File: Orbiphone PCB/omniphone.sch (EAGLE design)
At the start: 45 parts

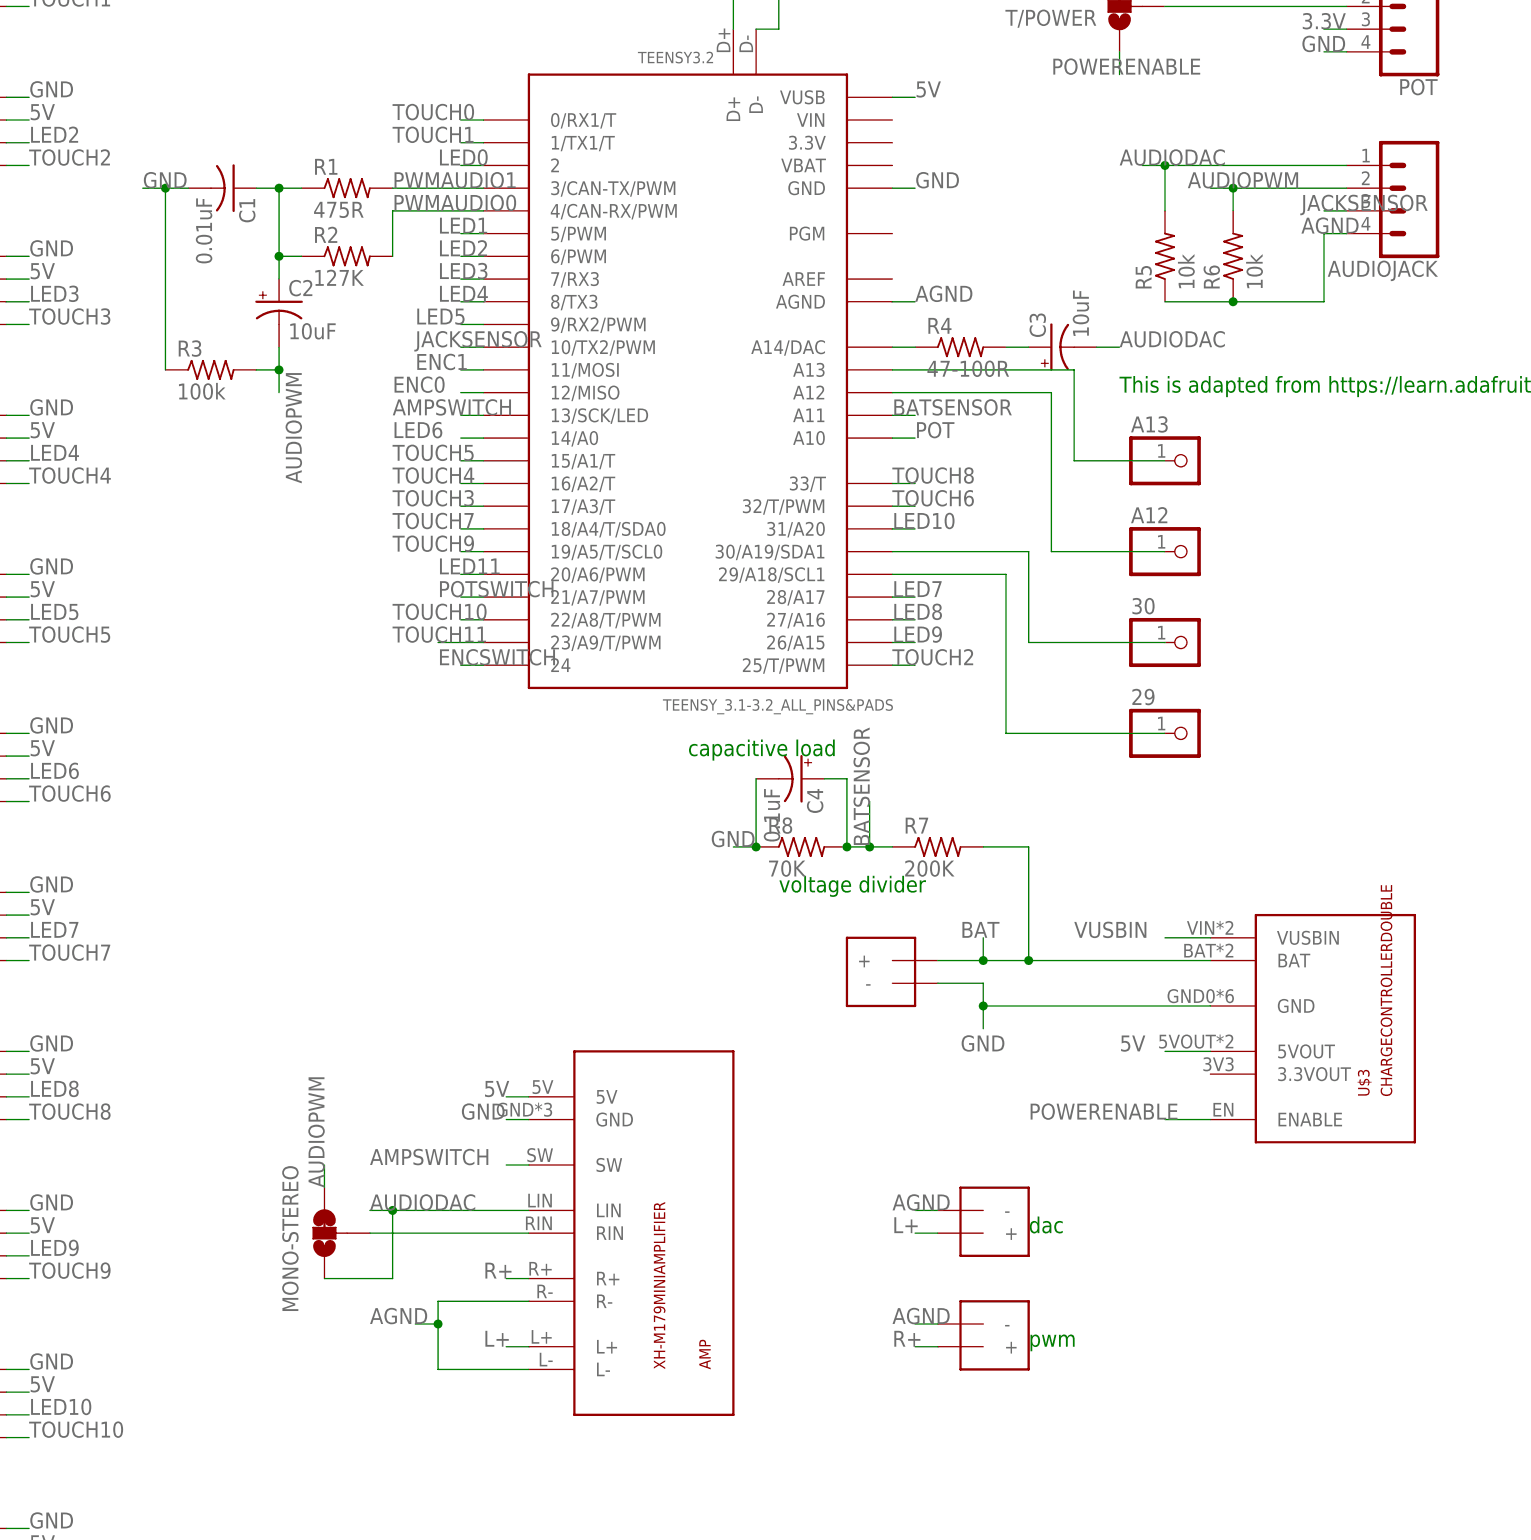
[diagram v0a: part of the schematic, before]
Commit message: added speaker and headphone fixes
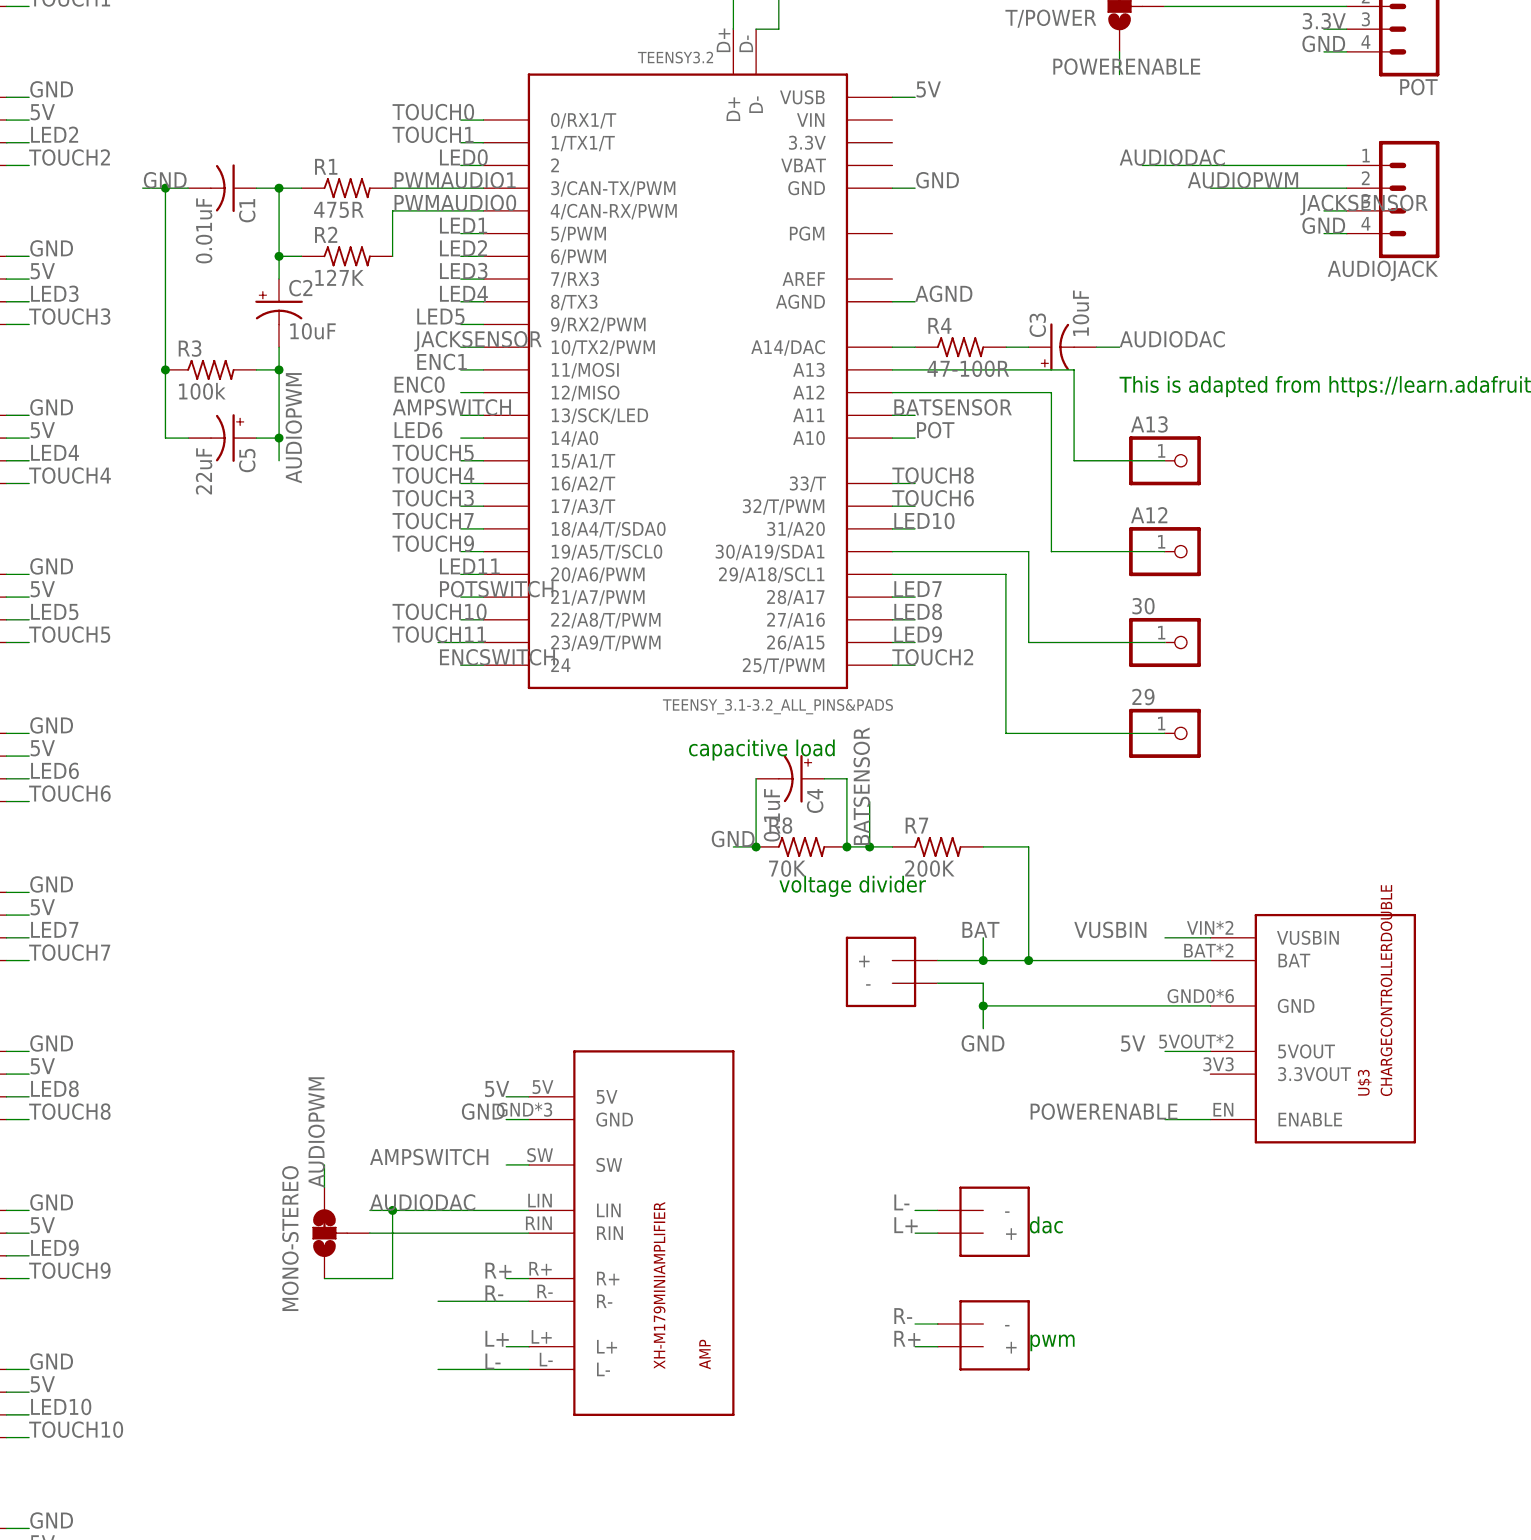
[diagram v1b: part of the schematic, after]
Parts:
- removed R5, R6: 10k, adafruit:R-US_0204/2V
- added C5: 22uF, adafruit:CPOL-USE2-4
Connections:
- new net L-: AMP.L-, SPEAKERDAC.-
- new net R-: AMP.R-, SPEAKERPWM.-
- net AGND: no longer AMP.L-, AMP.R-, AUDIOJACK.4, R5.1, R6.1, SPEAKERDAC.-, SPEAKERPWM.-
- net AUDIODAC: no longer R5.2
- net AUDIOPWM: now also C5.+; no longer R6.2
- net GND: now also AUDIOJACK.4, C5.-
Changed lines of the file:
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@@
 <part name="C3" library="adafruit" library_urn="urn:adsk.eagle:library:420" deviceset="CPOL-US" device="E2-4" package3d_urn="urn:adsk.eagle:package:6240495/1" value="10uF"/>
 <part name="R4" library="adafruit" library_urn="urn:adsk.eagle:library:420" deviceset="R-US_" device="0204/2V" package3d_urn="urn:adsk.eagle:package:6240630/1" value="47-100R"/>
-<part name="R5" library="adafruit" library_urn="urn:adsk.eagle:library:420" deviceset="R-US_" device="0204/2V" package3d_urn="urn:adsk.eagle:package:6240630/1" value="10k"/>
-<part name="R6" library="adafruit" library_urn="urn:adsk.eagle:library:420" deviceset="R-US_" device="0204/2V" package3d_urn="urn:adsk.eagle:package:6240630/1" value="10k"/>
 <part name="MONO-STEREO" library="SparkFun-Jumpers" library_urn="urn:adsk.eagle:library:528" deviceset="JUMPER-SMT_3_1-NC_TRACE" device="_SILK" package3d_urn="urn:adsk.eagle:package:39288/1"/>
 <part name="SPEAKERDAC" library="ArvidLibrary" deviceset="SPEAKERTERMINAL" device="-3.5MM" package3d_urn="urn:adsk.eagle:package:6240635/1"/>
@@
 <part name="30" library="adafruit" library_urn="urn:adsk.eagle:library:420" deviceset="PINHD-1X1" device="" package3d_urn="urn:adsk.eagle:package:6240654/1"/>
 <part name="29" library="adafruit" library_urn="urn:adsk.eagle:library:420" deviceset="PINHD-1X1" device="" package3d_urn="urn:adsk.eagle:package:6240654/1"/>
+<part name="C5" library="adafruit" library_urn="urn:adsk.eagle:library:420" deviceset="CPOL-US" device="E2-4" package3d_urn="urn:adsk.eagle:package:6240495/1" value="22uF"/>
 </parts>
 <sheets>
@@
 <attribute name="VALUE" x="90.17" y="60.198" size="1.778" layer="96"/>
 </instance>
-<instance part="R5" gate="G$1" x="116.84" y="73.66" smashed="yes" rot="R90">
-<attribute name="NAME" x="115.3414" y="69.85" size="1.778" layer="95" rot="R90"/>
-<attribute name="VALUE" x="120.142" y="69.85" size="1.778" layer="96" rot="R90"/>
-</instance>
-<instance part="R6" gate="G$1" x="124.46" y="73.66" smashed="yes" rot="R90">
-<attribute name="NAME" x="122.9614" y="69.85" size="1.778" layer="95" rot="R90"/>
-<attribute name="VALUE" x="127.762" y="69.85" size="1.778" layer="96" rot="R90"/>
-</instance>
 <instance part="MONO-STEREO" gate="G$1" x="22.86" y="-35.56" smashed="yes" rot="R180">
 <attribute name="NAME" x="18.161" y="-27.94" size="1.778" layer="95" font="vector" rot="R270"/>
@@
 <attribute name="NAME" x="113.03" y="23.495" size="1.778" layer="95"/>
 <attribute name="VALUE" x="113.03" y="15.24" size="1.778" layer="96"/>
+</instance>
+<instance part="C5" gate="G$1" x="12.7" y="53.34" smashed="yes" rot="R270">
+<attribute name="NAME" x="13.335" y="52.324" size="1.778" layer="95" rot="R270"/>
+<attribute name="VALUE" x="8.509" y="52.324" size="1.778" layer="96" rot="R270"/>
 </instance>
 </instances>
@@
 <junction x="5.08" y="81.28"/>
 <label x="2.54" y="81.28" size="1.778" layer="95"/>
+<pinref part="C5" gate="G$1" pin="-"/>
+<wire x1="7.62" y1="53.34" x2="5.08" y2="53.34" width="0.1524" layer="91"/>
+<wire x1="5.08" y1="53.34" x2="5.08" y2="60.96" width="0.1524" layer="91"/>
+<junction x="5.08" y="60.96"/>
 </segment>
 <segment>
@@
 <wire x1="71.12" y1="15.24" x2="71.12" y2="7.62" width="0.1524" layer="91"/>
 <junction x="71.12" y="7.62"/>
+</segment>
+<segment>
+<pinref part="AUDIOJACK" gate="G$1" pin="4"/>
+<wire x1="137.16" y1="76.2" x2="134.62" y2="76.2" width="0.1524" layer="91"/>
+<label x="132.08" y="76.2" size="1.778" layer="95"/>
 </segment>
 </net>
@@
 <pinref part="C2" gate="G$1" pin="-"/>
 <wire x1="17.78" y1="63.5" x2="17.78" y2="60.96" width="0.1524" layer="91"/>
-<wire x1="17.78" y1="60.96" x2="17.78" y2="58.42" width="0.1524" layer="91"/>
 <wire x1="17.78" y1="60.96" x2="15.24" y2="60.96" width="0.1524" layer="91"/>
 <junction x="17.78" y="60.96"/>
 <pinref part="R3" gate="G$1" pin="2"/>
 <label x="20.32" y="48.26" size="1.778" layer="95" rot="R90"/>
+<pinref part="C5" gate="G$1" pin="+"/>
+<wire x1="17.78" y1="60.96" x2="17.78" y2="53.34" width="0.1524" layer="91"/>
+<wire x1="17.78" y1="53.34" x2="15.24" y2="53.34" width="0.1524" layer="91"/>
+<wire x1="17.78" y1="53.34" x2="17.78" y2="50.8" width="0.1524" layer="91"/>
+<junction x="17.78" y="53.34"/>
 </segment>
 <segment>
 <pinref part="AUDIOJACK" gate="G$1" pin="2"/>
 <label x="119.38" y="81.28" size="1.778" layer="95"/>
-<pinref part="R6" gate="G$1" pin="2"/>
-<wire x1="137.16" y1="81.28" x2="124.46" y2="81.28" width="0.1524" layer="91"/>
-<wire x1="124.46" y1="81.28" x2="124.46" y2="78.74" width="0.1524" layer="91"/>
-<wire x1="124.46" y1="81.28" x2="121.92" y2="81.28" width="0.1524" layer="91"/>
-<junction x="124.46" y="81.28"/>
+<wire x1="137.16" y1="81.28" x2="121.92" y2="81.28" width="0.1524" layer="91"/>
 </segment>
 <segment>
@@
 <pinref part="AUDIOJACK" gate="G$1" pin="1"/>
 <label x="111.76" y="83.82" size="1.778" layer="95"/>
-<pinref part="R5" gate="G$1" pin="2"/>
-<wire x1="137.16" y1="83.82" x2="116.84" y2="83.82" width="0.1524" layer="91"/>
-<wire x1="116.84" y1="83.82" x2="116.84" y2="78.74" width="0.1524" layer="91"/>
-<wire x1="116.84" y1="83.82" x2="114.3" y2="83.82" width="0.1524" layer="91"/>
-<junction x="116.84" y="83.82"/>
+<wire x1="137.16" y1="83.82" x2="114.3" y2="83.82" width="0.1524" layer="91"/>
 </segment>
 <segment>
@@
 <wire x1="86.36" y1="68.58" x2="88.9" y2="68.58" width="0.1524" layer="91"/>
 <label x="88.9" y="68.58" size="1.778" layer="95"/>
-</segment>
-<segment>
-<pinref part="AMP" gate="G$1" pin="L-"/>
-<wire x1="45.72" y1="-50.8" x2="35.56" y2="-50.8" width="0.1524" layer="91"/>
-<pinref part="AMP" gate="G$1" pin="R-"/>
-<wire x1="35.56" y1="-50.8" x2="35.56" y2="-45.72" width="0.1524" layer="91"/>
-<wire x1="35.56" y1="-45.72" x2="35.56" y2="-43.18" width="0.1524" layer="91"/>
-<wire x1="35.56" y1="-43.18" x2="45.72" y2="-43.18" width="0.1524" layer="91"/>
-<wire x1="35.56" y1="-45.72" x2="33.02" y2="-45.72" width="0.1524" layer="91"/>
-<junction x="35.56" y="-45.72"/>
-<label x="27.94" y="-45.72" size="1.778" layer="95"/>
-</segment>
-<segment>
-<pinref part="AUDIOJACK" gate="G$1" pin="4"/>
-<wire x1="137.16" y1="76.2" x2="134.62" y2="76.2" width="0.1524" layer="91"/>
-<label x="132.08" y="76.2" size="1.778" layer="95"/>
-<pinref part="R6" gate="G$1" pin="1"/>
-<wire x1="124.46" y1="68.58" x2="134.62" y2="68.58" width="0.1524" layer="91"/>
-<wire x1="134.62" y1="68.58" x2="134.62" y2="76.2" width="0.1524" layer="91"/>
-<pinref part="R5" gate="G$1" pin="1"/>
-<wire x1="124.46" y1="68.58" x2="116.84" y2="68.58" width="0.1524" layer="91"/>
-<junction x="124.46" y="68.58"/>
-</segment>
-<segment>
-<pinref part="SPEAKERPWM" gate="&gt;NAME" pin="-"/>
-<wire x1="91.44" y1="-45.72" x2="88.9" y2="-45.72" width="0.1524" layer="91"/>
-<label x="86.36" y="-45.72" size="1.778" layer="95"/>
-</segment>
-<segment>
-<pinref part="SPEAKERDAC" gate="&gt;NAME" pin="-"/>
-<wire x1="91.44" y1="-33.02" x2="88.9" y2="-33.02" width="0.1524" layer="91"/>
-<label x="86.36" y="-33.02" size="1.778" layer="95"/>
 </segment>
 </net>
@@
 </segment>
 </net>
+<net name="R-" class="0">
+<segment>
+<pinref part="AMP" gate="G$1" pin="R-"/>
+<wire x1="35.56" y1="-43.18" x2="45.72" y2="-43.18" width="0.1524" layer="91"/>
+<label x="40.64" y="-43.18" size="1.778" layer="95"/>
+</segment>
+<segment>
+<pinref part="SPEAKERPWM" gate="&gt;NAME" pin="-"/>
+<wire x1="91.44" y1="-45.72" x2="88.9" y2="-45.72" width="0.1524" layer="91"/>
+<label x="86.36" y="-45.72" size="1.778" layer="95"/>
+</segment>
+</net>
+<net name="L-" class="0">
+<segment>
+<pinref part="AMP" gate="G$1" pin="L-"/>
+<wire x1="45.72" y1="-50.8" x2="35.56" y2="-50.8" width="0.1524" layer="91"/>
+<label x="40.64" y="-50.8" size="1.778" layer="95"/>
+</segment>
+<segment>
+<pinref part="SPEAKERDAC" gate="&gt;NAME" pin="-"/>
+<wire x1="91.44" y1="-33.02" x2="88.9" y2="-33.02" width="0.1524" layer="91"/>
+<label x="86.36" y="-33.02" size="1.778" layer="95"/>
+</segment>
+</net>
